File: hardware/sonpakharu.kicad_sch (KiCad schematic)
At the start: 62 parts, among them IC1 ESP32-S3-WROOM-1U-N4, J1 ADC4, J10 EXT2, J11 EXT3, J12 BATT, J13 EXT7, J14 PWR, J15 EXT8, J16 FTDI, J17 485, J2 ADC3, J3 ADC2, J4 ADC1, J5 EXT4, J6 I2C, J7 EXT5, J8 EXT1, J9 EXT6, Q1 DMG3415U, Q2 S8050, Q3 S8050, Q4 S8050, SW1 Boot, SW2 Reset, U1 AP2112K-3.3TRG1, U2 MCP73831-2-OT, U3 ADS1115IDGSR, U4 MAX485E

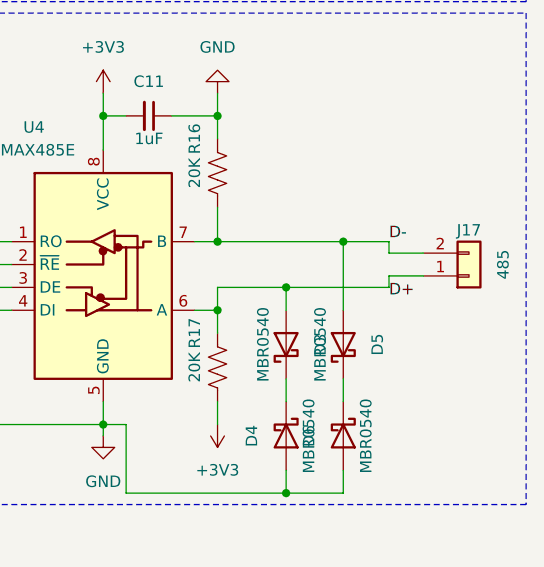
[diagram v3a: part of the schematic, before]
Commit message: component placment done
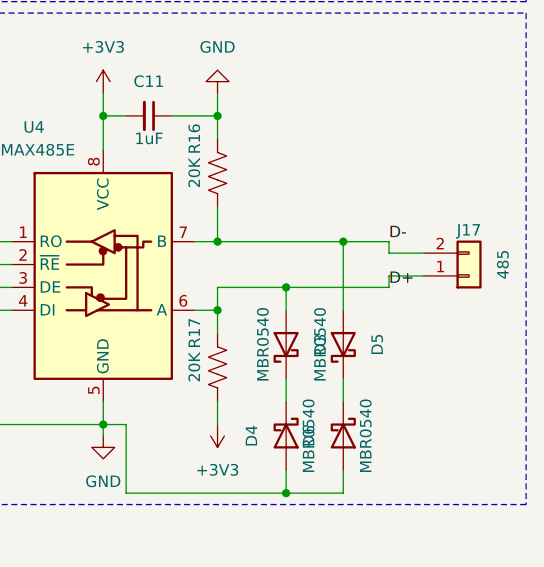
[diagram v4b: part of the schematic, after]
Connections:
- net D+: now also D3.2 (A), J17.1 (Pin_1), R17.1, U4.6 (A)
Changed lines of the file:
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@@
     (effects (font (size 1.27 1.27)) (justify left bottom))
   )
-  (label "D+" (at 266.7 142.24 0) (fields_autoplaced)
+  (label "D+" (at 266.7 140.97 0) (fields_autoplaced)
     (effects (font (size 1.27 1.27)) (justify left bottom))
   )

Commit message: almost all tracks corrected, added tactile smd
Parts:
- SW1, SW2: footprint Button_Switch_THT:SW_Tactile_Straight_KSA0Axx1LFTR -> Button_Switch_SMD:SW_Push_1P1T_NO_6x6mm_H9.5mm
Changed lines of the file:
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@@
       (effects (font (size 1.27 1.27)) (justify left))
     )
-    (property "Footprint" "Button_Switch_THT:SW_Tactile_Straight_KSA0Axx1LFTR" (at 78.74 133.35 0)
+    (property "Footprint" "Button_Switch_SMD:SW_Push_1P1T_NO_6x6mm_H9.5mm" (at 78.74 133.35 0)
       (effects (font (size 1.27 1.27)) hide)
     )
@@
       (effects (font (size 1.27 1.27)) (justify left))
     )
-    (property "Footprint" "Button_Switch_THT:SW_Tactile_Straight_KSA0Axx1LFTR" (at 67.31 133.35 0)
-      (effects (font (size 1.27 1.27)) hide)
-    )
+    (property "Footprint" "Button_Switch_SMD:SW_Push_1P1T_NO_6x6mm_H9.5mm" (at 67.31 133.35 0)
+      (effects (font (size 1.27 1.27)) hide)
+    )

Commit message: completed all labels, added mx485 mpn
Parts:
- U4: MPN (none) -> C19738
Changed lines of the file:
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@@
+      (effects (font (size 1.27 1.27)) hide)
+    )
+    (property "MPN" "C19738" (at 234.95 138.43 0)
       (effects (font (size 1.27 1.27)) hide)
     )

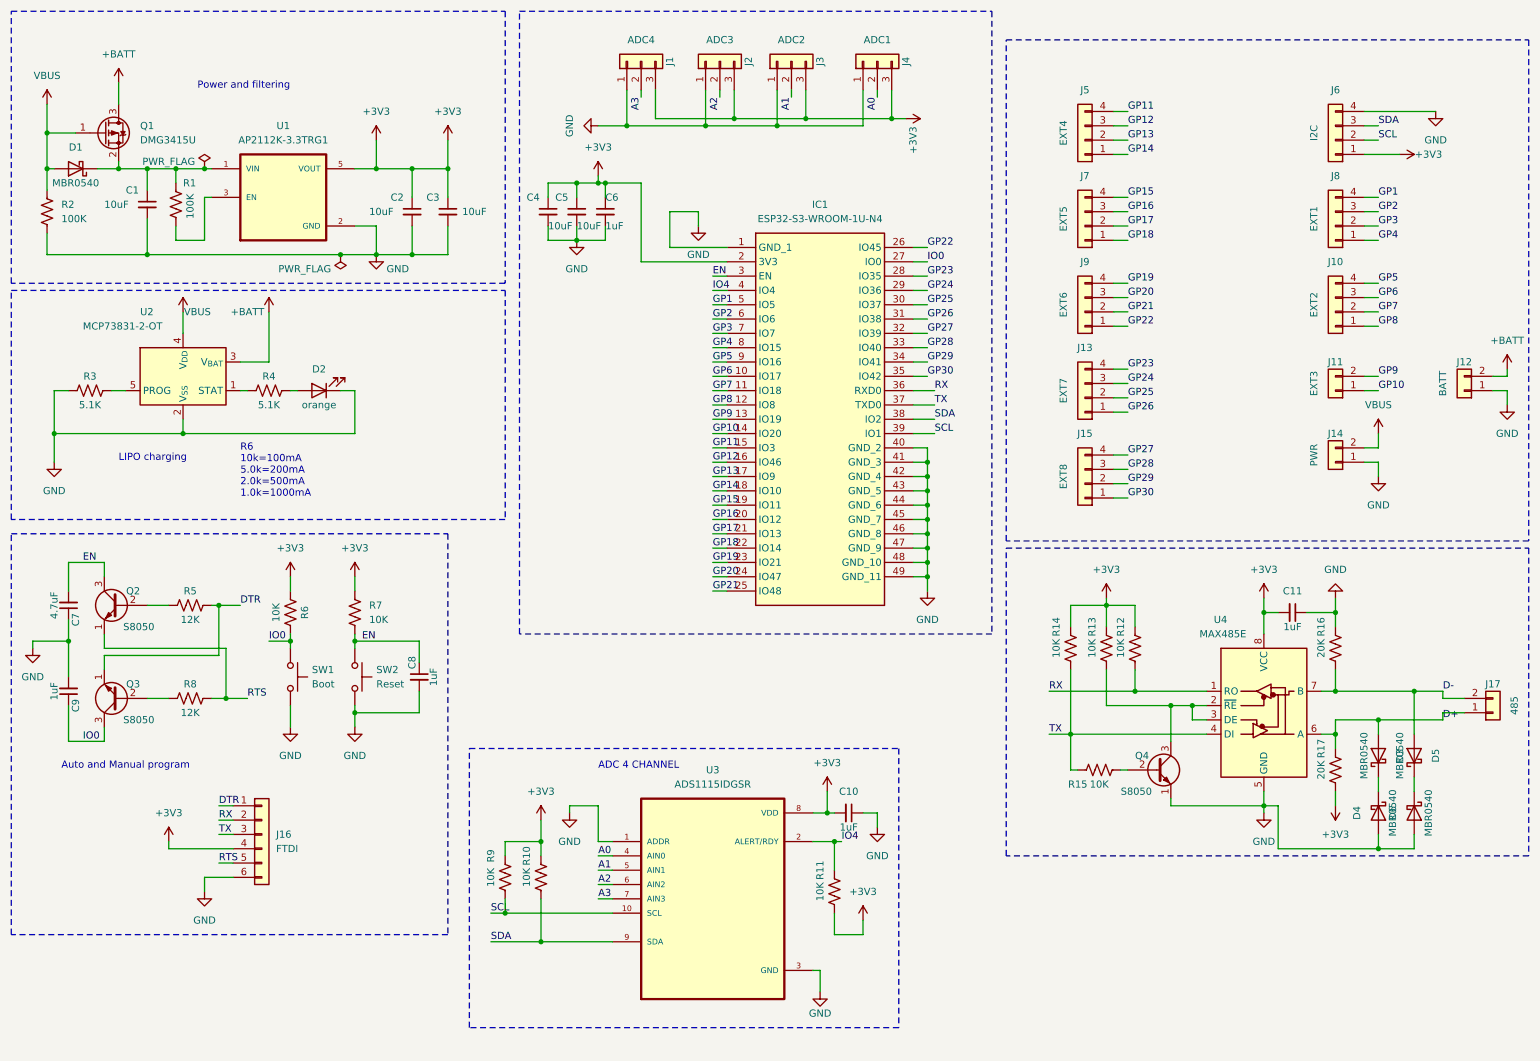
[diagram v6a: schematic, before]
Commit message: Fix: added pads, ground vias and logo
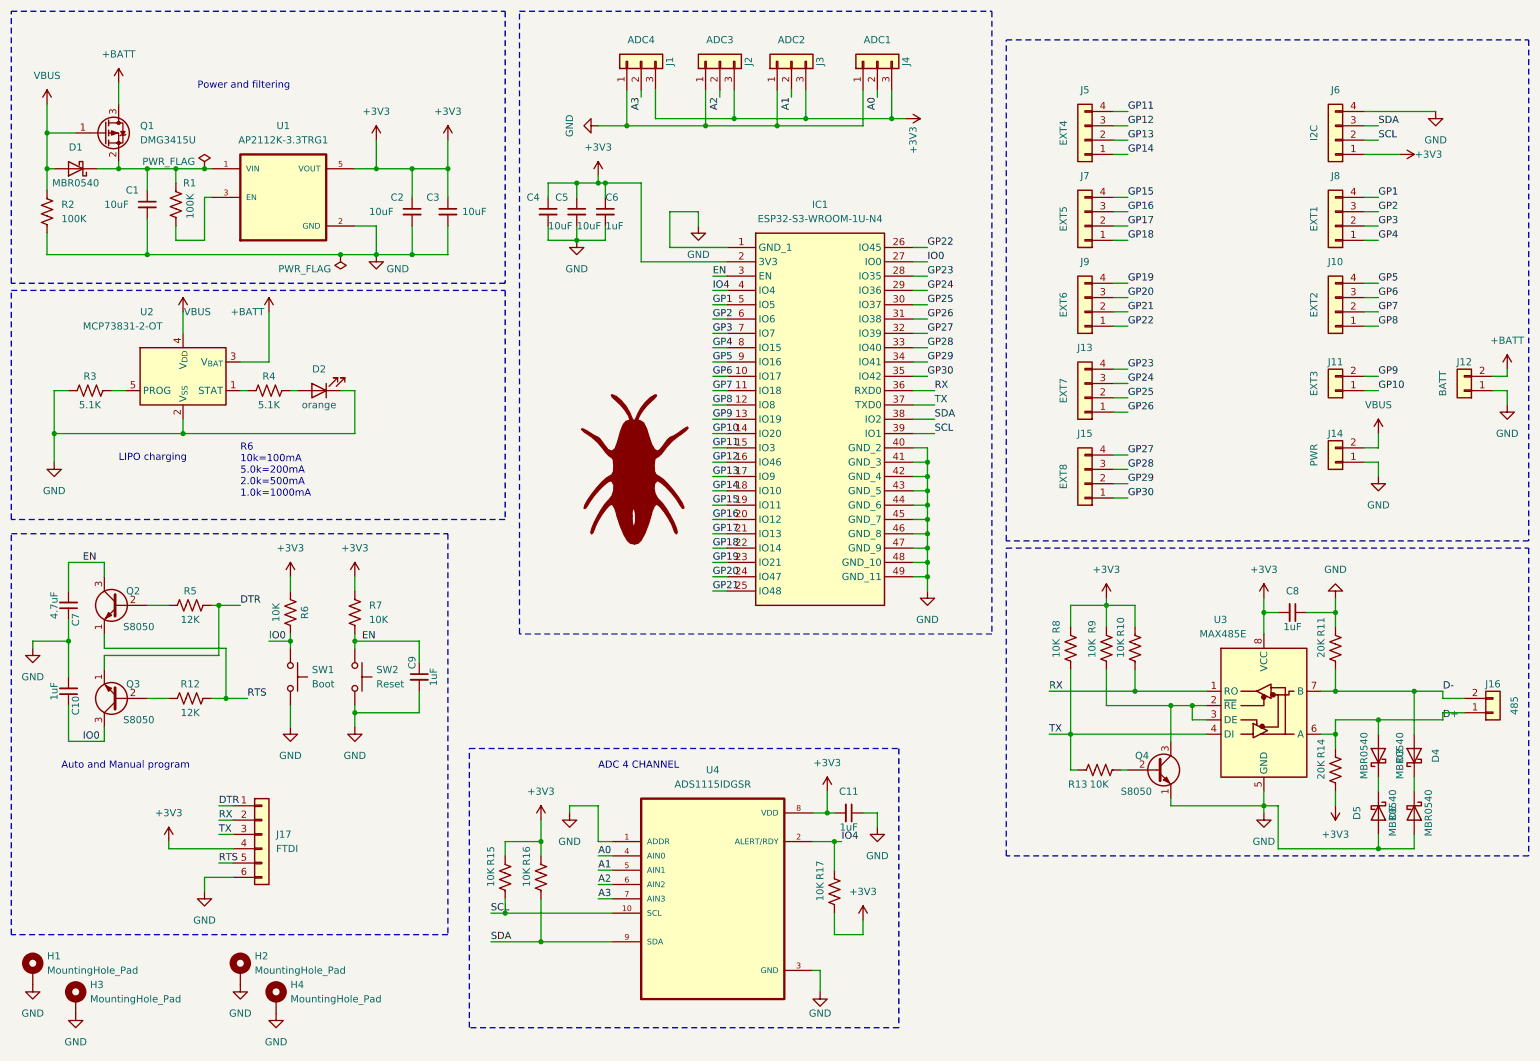
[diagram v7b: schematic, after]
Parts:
- added H1, H2, H3: MountingHole_Pad, MountingHole:MountingHole_2.2mm_M2_Pad_Via, symbol Mechanical:MountingHole_Pad
- added H4: MountingHole_Pad, MountingHole:MountingHole_2.2mm_M2_DIN965_Pad, symbol Mechanical:MountingHole_Pad
- IC1: footprint RF_Module:ESP32S3WROOM1UN4 -> KiCad:ESP32S3WROOM1UN4
- U3: renamed from U4; footprint MAX485SOIC8:21-0041B_8_MXM -> Package_SO:SOP-8_3.9x4.9mm_P1.27mm
- renumbered C9 to C10, C10 to C11, C11 to C8, C8 to C9, D5 to D4, D4 to D5, J17 to J16, J16 to J17, R12 to R10, R16 to R11, R8 to R12, R15 to R13, R17 to R14, R9 to R15, R10 to R16, R11 to R17, R14 to R8, R13 to R9, U3 to U4
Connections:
- net GND: now also H1.1, H2.1, H3.1, H4.1

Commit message: updated tactile smd part number
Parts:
- SW1, SW2: MPN C116647 -> C285446
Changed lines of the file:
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@@
       (effects (font (size 1.27 1.27)) hide)
     )
-    (property "MPN" "C116647" (at 73.66 133.35 0)
+    (property "MPN" "C285446" (at 73.66 133.35 0)
       (effects (font (size 1.27 1.27)) hide)
     )
@@
       (effects (font (size 1.27 1.27)) hide)
     )
-    (property "MPN" "C116647" (at 62.23 133.35 0)
-      (effects (font (size 1.27 1.27)) hide)
-    )
+    (property "MPN" "C285446" (at 62.23 133.35 0)
+      (effects (font (size 1.27 1.27)) hide)
+    )
